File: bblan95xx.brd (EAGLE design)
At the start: 50 x 50 mm, 52 parts, among them IC1 LAN9512, IC2 93ST, Q1 25MHz

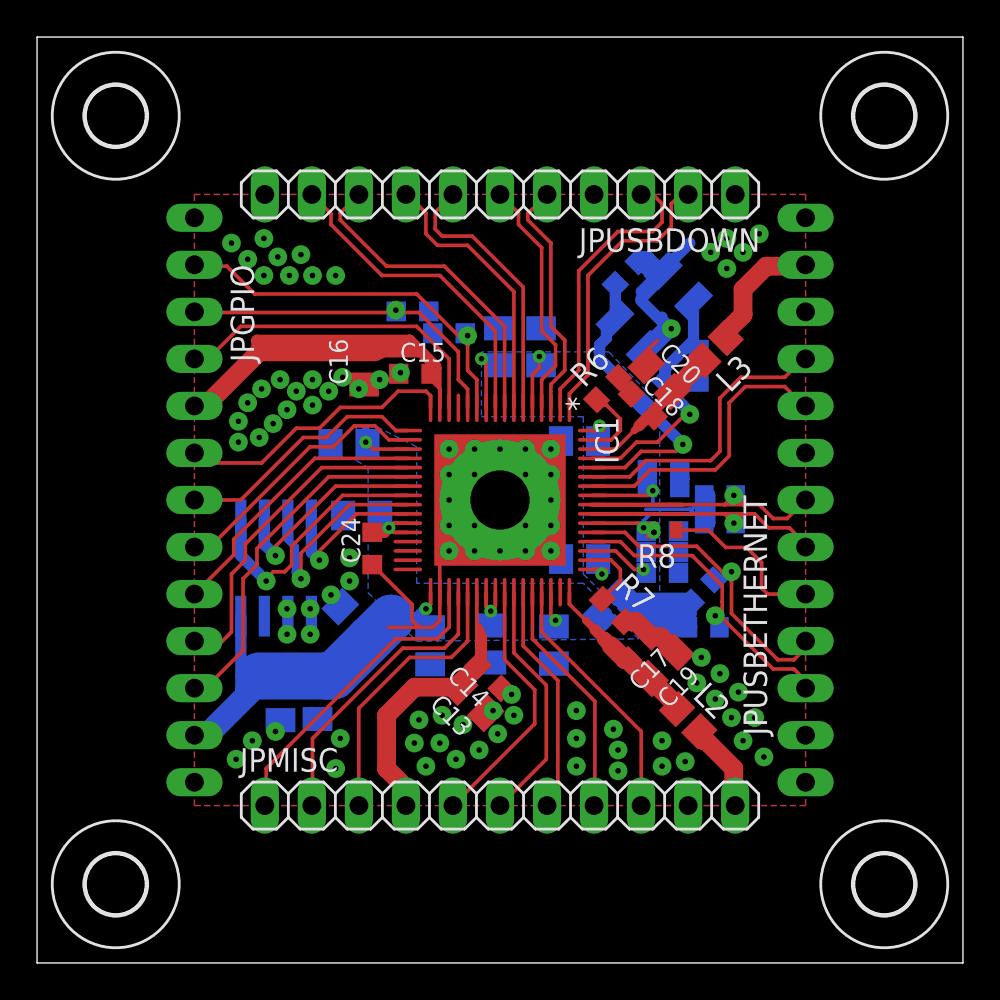
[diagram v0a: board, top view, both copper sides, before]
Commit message: mirror pinjumper headers try two
Mirror and rotate JPUSBDOWN and JPMISC

Signed-off-by: Stephan Baerwolf <stephan@matrixstorm.com>
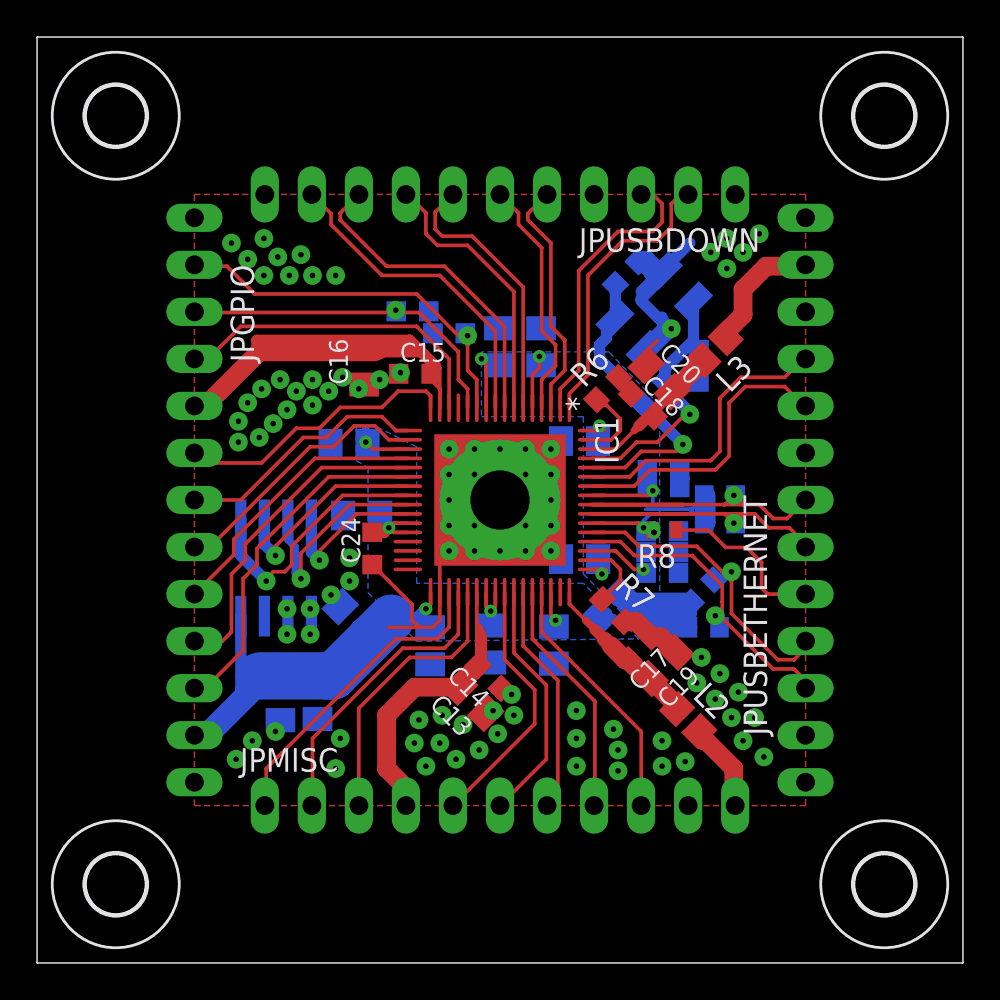
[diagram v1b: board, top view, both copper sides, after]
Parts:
- flipped JPMISC to the bottom, turned to 180 degrees
- flipped JPUSBDOWN to the bottom, turned to 0 degrees
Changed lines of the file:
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@@
 <element name="H3" library="holes" package="3,2" value="MOUNT-HOLE3.2" x="4.25" y="4.25"/>
 <element name="H4" library="holes" package="3,2" value="MOUNT-HOLE3.2" x="45.75" y="4.25"/>
-<element name="JPUSBDOWN" library="pinhead" package="1X11" value="" x="25" y="41.5" rot="R180"/>
+<element name="JPUSBDOWN" library="pinhead" package="1X11" value="" x="25" y="41.5" smashed="yes" rot="MR0">
+<attribute name="NAME" x="39.0462" y="39.6712" size="1.27" layer="25" ratio="10" rot="R180"/>
+<attribute name="VALUE" x="38.97" y="44.675" size="1.27" layer="27" rot="R180"/>
+</element>
 <element name="JPGPIO" library="pinhead" package="1X13" value="" x="8.5" y="25" smashed="yes" rot="MR270">
 <attribute name="NAME" x="10.4538" y="37.7112" size="1.27" layer="25" ratio="10" rot="R270"/>
 <attribute name="VALUE" x="5.325" y="41.51" size="1.27" layer="27" rot="R270"/>
 </element>
-<element name="JPMISC" library="pinhead" package="1X11" value="" x="25" y="8.5" rot="R0"/>
+<element name="JPMISC" library="pinhead" package="1X11" value="" x="25" y="8.5" smashed="yes" rot="MR180">
+<attribute name="NAME" x="10.9538" y="10.3288" size="1.27" layer="25" ratio="10"/>
+<attribute name="VALUE" x="11.03" y="5.325" size="1.27" layer="27"/>
+</element>
 <element name="JPUSBETHERNET" library="pinhead" package="1X13" value="" x="41.5" y="25" smashed="yes" rot="MR90">
 <attribute name="NAME" x="39.4212" y="12.2888" size="1.27" layer="25" ratio="10" rot="R90"/>
